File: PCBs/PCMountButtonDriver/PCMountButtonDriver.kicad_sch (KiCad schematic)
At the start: 12 parts, among them U1 74HC164

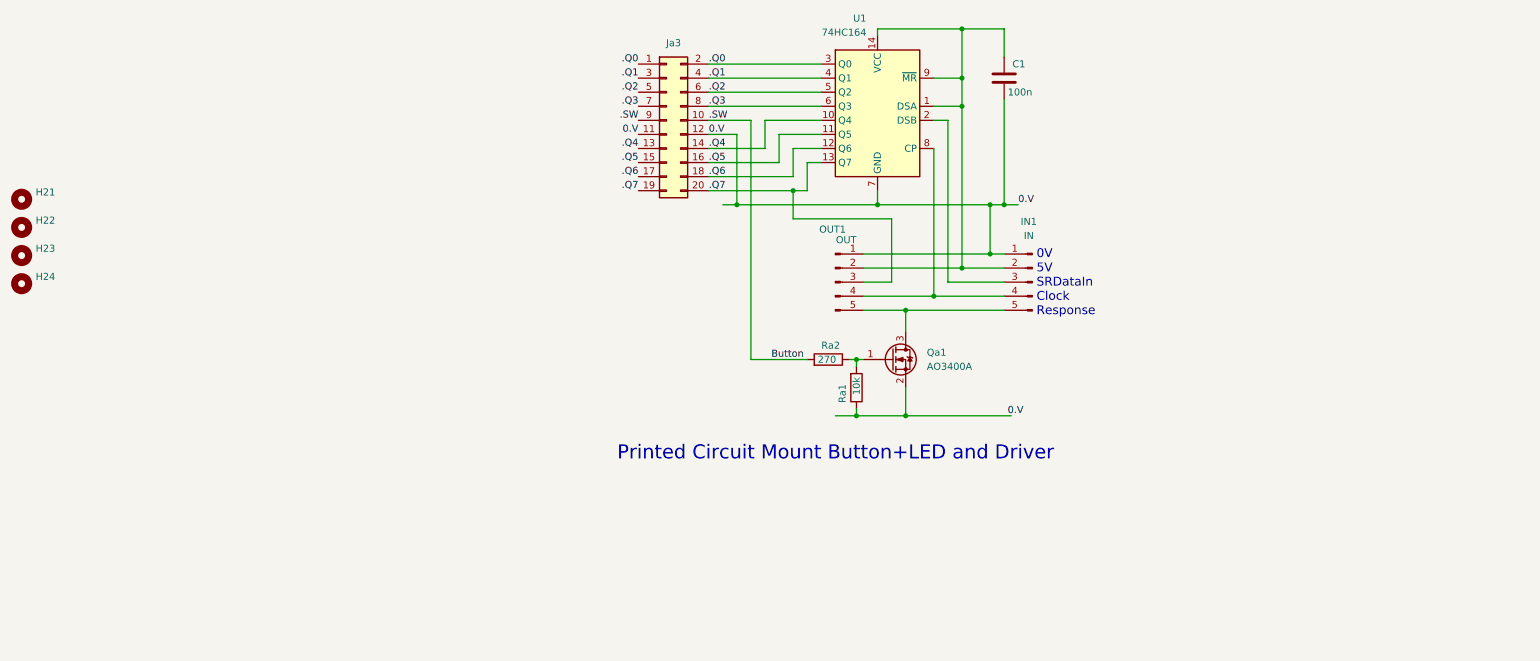
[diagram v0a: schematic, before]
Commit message: V1.1 PCB updates after initial testing 1. Share data out line between LCD, 7 Segment and button scan to yield spare io lines for    control of WS8212 LEDs for music stand lamp 2. Replace level shifting FET on Button Driver PCBs by resistor 3. Generate combined ks61,button driver & button mount prototype PCB for economic testing with JLC PCB
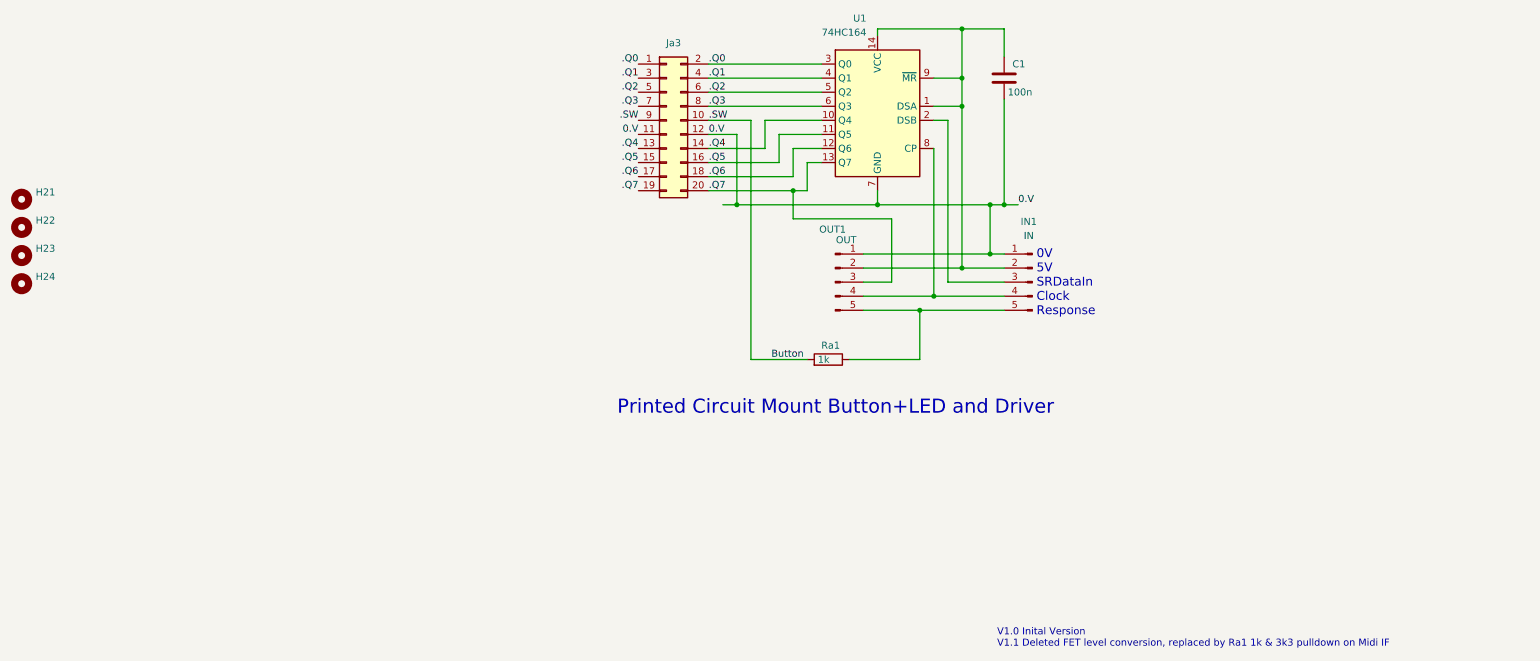
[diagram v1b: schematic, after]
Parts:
- removed Qa1: AO3400A, Package_TO_SOT_SMD:SOT-23, symbol Transistor_FET:AO3400A
- removed Ra1: 10k, Resistor_SMD:R_0805_2012Metric_Pad1.20x1.40mm_HandSolder, symbol Device:R
- Ra1: renamed from Ra2; value 270 -> 1k
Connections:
- net at IN1.5 (Pin_5), OUT1.5 (Pin_5): now also Ra1.1
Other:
- note added: "V1.0 Inital Version V1.1 Deleted FET level conversion, replaced by Ra1 1k & 3k3 pulldown on Midi IF"
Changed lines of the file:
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@@
   (junction (at 177.8 100.33) (diameter 0) (color 0 0 0 0)
   )
-  (junction (at 153.67 129.54) (diameter 0) (color 0 0 0 0)
-  )
-  (junction (at 162.56 129.54) (diameter 0) (color 0 0 0 0)
-  )
-  (junction (at 153.67 119.38) (diameter 0) (color 0 0 0 0)
-  )
   (junction (at 172.72 73.66) (diameter 0) (color 0 0 0 0)
   )
@@
   (junction (at 177.8 91.44) (diameter 0) (color 0 0 0 0)
   )
-  (junction (at 162.56 110.49) (diameter 0) (color 0 0 0 0)
-  )
   (junction (at 167.64 107.95) (diameter 0) (color 0 0 0 0)
   )
+  (junction (at 165.1 110.49) (diameter 0) (color 0 0 0 0)
+  )
   (wire (pts (xy 139.7 78.74) (xy 147.32 78.74))
     (stroke (width 0) (type default) (color 0 0 0 0))
@@
     (stroke (width 0) (type default) (color 0 0 0 0))
   )
-  (wire (pts (xy 153.67 119.38) (xy 152.4 119.38))
-    (stroke (width 0) (type default) (color 0 0 0 0))
-  )
   (wire (pts (xy 142.24 88.9) (xy 142.24 93.98))
     (stroke (width 0) (type default) (color 0 0 0 0))
@@
     (stroke (width 0) (type default) (color 0 0 0 0))
   )
+  (wire (pts (xy 165.1 110.49) (xy 165.1 119.38))
+    (stroke (width 0) (type default) (color 0 0 0 0))
+  )
   (wire (pts (xy 167.64 73.66) (xy 172.72 73.66))
     (stroke (width 0) (type default) (color 0 0 0 0))
@@
     (stroke (width 0) (type default) (color 0 0 0 0))
   )
-  (wire (pts (xy 154.94 119.38) (xy 153.67 119.38))
-    (stroke (width 0) (type default) (color 0 0 0 0))
-  )
   (wire (pts (xy 134.62 76.2) (xy 134.62 119.38))
     (stroke (width 0) (type default) (color 0 0 0 0))
@@
     (stroke (width 0) (type default) (color 0 0 0 0))
   )
-  (wire (pts (xy 162.56 124.46) (xy 162.56 129.54))
-    (stroke (width 0) (type default) (color 0 0 0 0))
-  )
   (wire (pts (xy 182.88 91.44) (xy 180.34 91.44))
     (stroke (width 0) (type default) (color 0 0 0 0))
   )
+  (wire (pts (xy 165.1 119.38) (xy 152.4 119.38))
+    (stroke (width 0) (type default) (color 0 0 0 0))
+  )
   (wire (pts (xy 160.02 105.41) (xy 154.94 105.41))
     (stroke (width 0) (type default) (color 0 0 0 0))
   )
-  (wire (pts (xy 153.67 128.27) (xy 153.67 129.54))
-    (stroke (width 0) (type default) (color 0 0 0 0))
-  )
   (wire (pts (xy 167.64 107.95) (xy 180.34 107.95))
     (stroke (width 0) (type default) (color 0 0 0 0))
@@
     (stroke (width 0) (type default) (color 0 0 0 0))
   )
-  (wire (pts (xy 181.61 129.54) (xy 162.56 129.54))
-    (stroke (width 0) (type default) (color 0 0 0 0))
-  )
   (wire (pts (xy 142.24 88.9) (xy 144.78 88.9))
     (stroke (width 0) (type default) (color 0 0 0 0))
@@
     (stroke (width 0) (type default) (color 0 0 0 0))
   )
-  (wire (pts (xy 162.56 110.49) (xy 162.56 114.3))
-    (stroke (width 0) (type default) (color 0 0 0 0))
-  )
   (wire (pts (xy 180.34 91.44) (xy 177.8 91.44))
     (stroke (width 0) (type default) (color 0 0 0 0))
@@
     (stroke (width 0) (type default) (color 0 0 0 0))
   )
-  (wire (pts (xy 162.56 110.49) (xy 180.34 110.49))
-    (stroke (width 0) (type default) (color 0 0 0 0))
-  )
   (wire (pts (xy 167.64 81.28) (xy 167.64 107.95))
     (stroke (width 0) (type default) (color 0 0 0 0))
   )
-  (wire (pts (xy 154.94 110.49) (xy 162.56 110.49))
+  (wire (pts (xy 154.94 110.49) (xy 165.1 110.49))
     (stroke (width 0) (type default) (color 0 0 0 0))
   )
@@
     (stroke (width 0) (type default) (color 0 0 0 0))
   )
-  (wire (pts (xy 162.56 129.54) (xy 153.67 129.54))
-    (stroke (width 0) (type default) (color 0 0 0 0))
-  )
   (wire (pts (xy 144.78 83.82) (xy 147.32 83.82))
     (stroke (width 0) (type default) (color 0 0 0 0))
@@
     (stroke (width 0) (type default) (color 0 0 0 0))
   )
-  (wire (pts (xy 153.67 119.38) (xy 153.67 120.65))
-    (stroke (width 0) (type default) (color 0 0 0 0))
-  )
   (wire (pts (xy 154.94 107.95) (xy 167.64 107.95))
     (stroke (width 0) (type default) (color 0 0 0 0))
@@
     (stroke (width 0) (type default) (color 0 0 0 0))
   )
+  (wire (pts (xy 165.1 110.49) (xy 180.34 110.49))
+    (stroke (width 0) (type default) (color 0 0 0 0))
+  )
   (wire (pts (xy 172.72 73.66) (xy 172.72 102.87))
     (stroke (width 0) (type default) (color 0 0 0 0))
@@
     (stroke (width 0) (type default) (color 0 0 0 0))
   )
-  (wire (pts (xy 153.67 129.54) (xy 149.86 129.54))
-    (stroke (width 0) (type default) (color 0 0 0 0))
-  )
   (wire (pts (xy 170.18 105.41) (xy 180.34 105.41))
     (stroke (width 0) (type default) (color 0 0 0 0))
@@
     (stroke (width 0) (type default) (color 0 0 0 0))
   )
-  (text "Printed Circuit Mount Button+LED and Driver" (at 110.49 137.795 0)
+  (text "V1.0 Inital Version\nV1.1 Deleted FET level conversion, replaced by Ra1 1k & 3k3 pulldown on Midi IF"
+    (at 179.07 171.45 0)
+    (effects (font (size 1.27 1.27)) (justify left bottom))
+  )
+  (text "Printed Circuit Mount Button+LED and Driver" (at 110.49 129.54 0)
     (effects (font (size 2.54 2.54)) (justify left bottom))
   )
   (text "0V\n5V\nSRDataIn\nClock\nResponse" (at 186.182 111.633 0)
     (effects (font (size 1.6 1.6)) (justify left bottom))
-  )
-  (label "0.V" (at 180.975 129.54 0)
-    (effects (font (size 1.27 1.27)) (justify left bottom))
   )
   (label ".Q5" (at 127 83.82 0)
@@
   (symbol (lib_id "Device:R") (at 148.59 119.38 270) (mirror x) (unit 1)
     (in_bom yes) (on_board yes)
-    (property "Reference" "Ra2" (id 0) (at 147.32 116.84 90)
-      (effects (font (size 1.27 1.27)) (justify left))
-    )
-    (property "Value" "270" (id 1) (at 146.685 119.38 90)
+    (property "Reference" "Ra1" (id 0) (at 147.32 116.84 90)
+      (effects (font (size 1.27 1.27)) (justify left))
+    )
+    (property "Value" "1k" (id 1) (at 146.685 119.38 90)
       (effects (font (size 1.27 1.27)) (justify left))
     )
@@
     )
   )
-  (symbol (lib_id "Transistor_FET:AO3400A") (at 160.02 119.38 0) (unit 1)
-    (in_bom yes) (on_board yes) (fields_autoplaced)
-    (property "Reference" "Qa1" (id 0) (at 166.37 118.1099 0)
-      (effects (font (size 1.27 1.27)) (justify left))
-    )
-    (property "Value" "AO3400A" (id 1) (at 166.37 120.6499 0)
-      (effects (font (size 1.27 1.27)) (justify left))
-    )
-    (property "Footprint" "Package_TO_SOT_SMD:SOT-23" (id 2) (at 165.1 121.285 0)
-      (effects (font (size 1.27 1.27) italic) (justify left) hide)
-    )
-    (property "Datasheet" "http://www.aosmd.com/pdfs/datasheet/AO3400A.pdf" (id 3) (at 160.02 119.38 0)
-      (effects (font (size 1.27 1.27)) (justify left) hide)
-    )
-    (pin "1")
-    (pin "2")
-    (pin "3")
-  )
   (symbol (lib_id "74xx:74HC164") (at 157.48 73.66 0) (mirror y) (unit 1)
     (in_bom yes) (on_board yes) (fields_autoplaced)
@@
     (pin "5")
   )
-  (symbol (lib_id "Device:R") (at 153.67 124.46 0) (mirror x) (unit 1)
-    (in_bom yes) (on_board yes)
-    (property "Reference" "Ra1" (id 0) (at 151.13 123.825 90)
-      (effects (font (size 1.27 1.27)) (justify left))
-    )
-    (property "Value" "10k" (id 1) (at 153.67 122.555 90)
-      (effects (font (size 1.27 1.27)) (justify left))
-    )
-    (property "Footprint" "Resistor_SMD:R_0805_2012Metric_Pad1.20x1.40mm_HandSolder" (id 2) (at 151.892 124.46 90)
-      (effects (font (size 1.27 1.27)) hide)
-    )
-    (property "Datasheet" "~" (id 3) (at 153.67 124.46 0)
-      (effects (font (size 1.27 1.27)) hide)
-    )
-    (pin "1")
-    (pin "2")
-  )
   (sheet_instances
     (path "/" (page "1"))
@@
       (reference "OUT1") (unit 1) (value "OUT") (footprint "Connector_PinHeader_2.54mm:PinHeader_1x05_P2.54mm_Vertical")
     )
-    (path "/8558dab7-0d43-47de-80af-4cdd13781fe2"
-      (reference "Qa1") (unit 1) (value "AO3400A") (footprint "Package_TO_SOT_SMD:SOT-23")
-    )
-    (path "/fddeb50b-80e7-40f0-a80c-3e58c10d65bd"
-      (reference "Ra1") (unit 1) (value "10k") (footprint "Resistor_SMD:R_0805_2012Metric_Pad1.20x1.40mm_HandSolder")
-    )
     (path "/75af4dbc-432c-4b78-af1c-8859a57316d9"
-      (reference "Ra2") (unit 1) (value "270") (footprint "Resistor_SMD:R_0805_2012Metric_Pad1.20x1.40mm_HandSolder")
+      (reference "Ra1") (unit 1) (value "1k") (footprint "Resistor_SMD:R_0805_2012Metric_Pad1.20x1.40mm_HandSolder")
     )
     (path "/8564cc69-9a4b-408d-80ba-446914b3b830"
